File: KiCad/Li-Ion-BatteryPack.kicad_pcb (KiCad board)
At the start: 2 copper layers, 163.5 x 85.6 mm, 20 parts, among them J1 Charger, J2 Load, J3 Parallel, J4 BMS Sensor

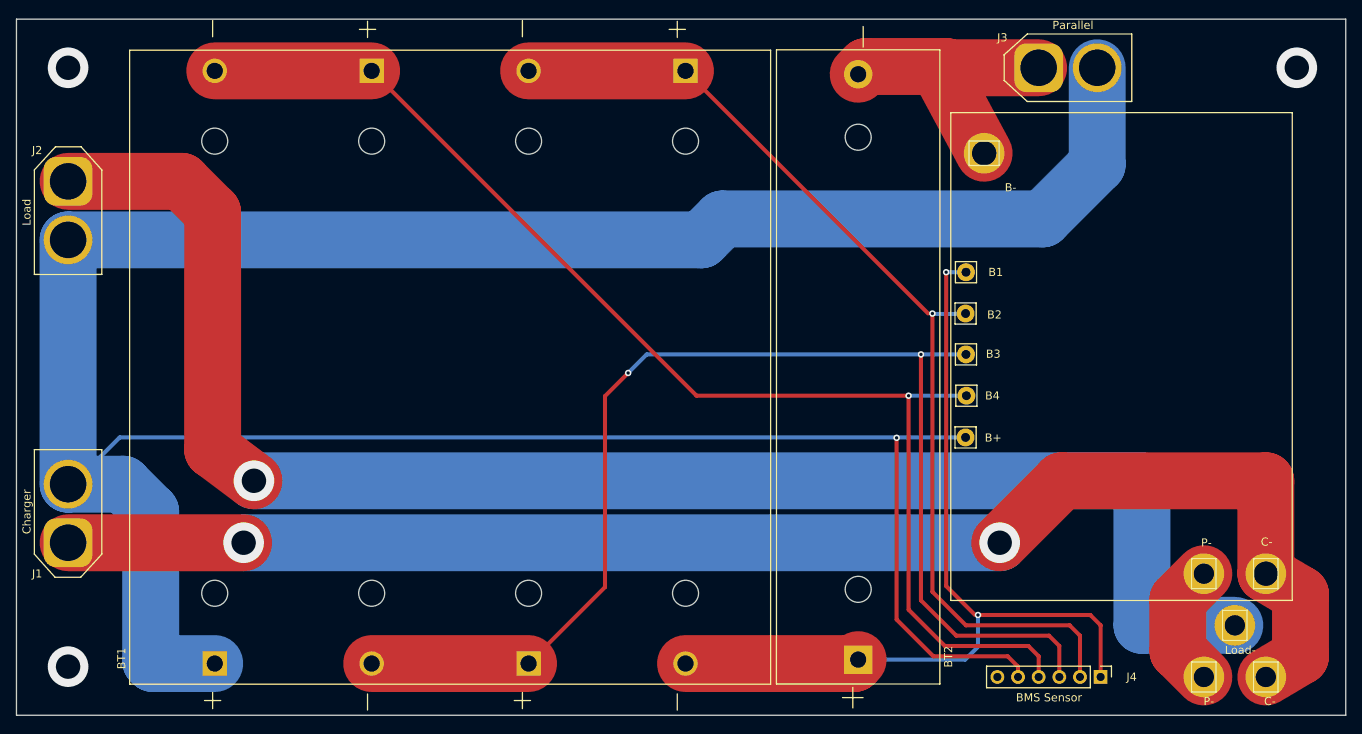
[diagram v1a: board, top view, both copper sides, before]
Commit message: Added some silkscreen objects to give better hints on wirering.
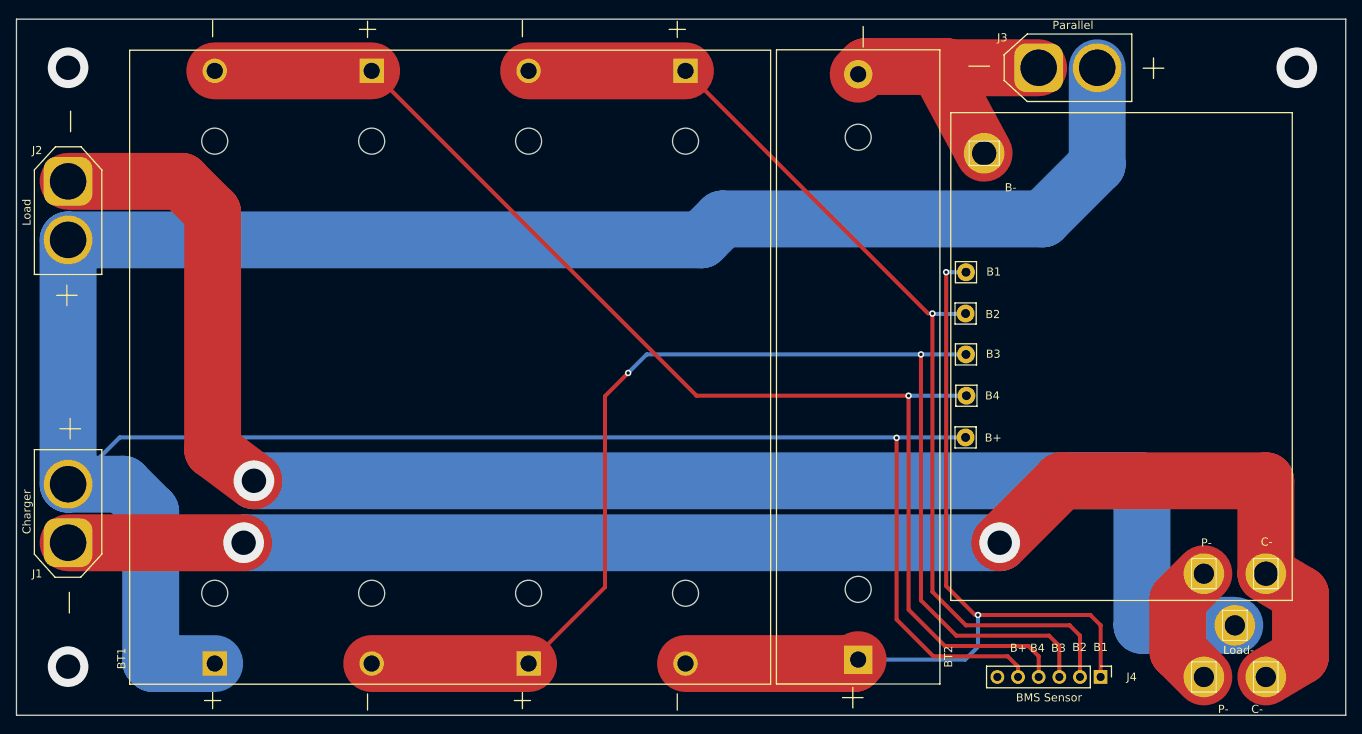
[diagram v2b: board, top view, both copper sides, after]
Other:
- board text added: "B+"
- board text added: "B1"
- board text added: "B2"
- board text added: "B3"
- board text added: "B4"

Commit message: Flipped some high current connections to the back of the board.
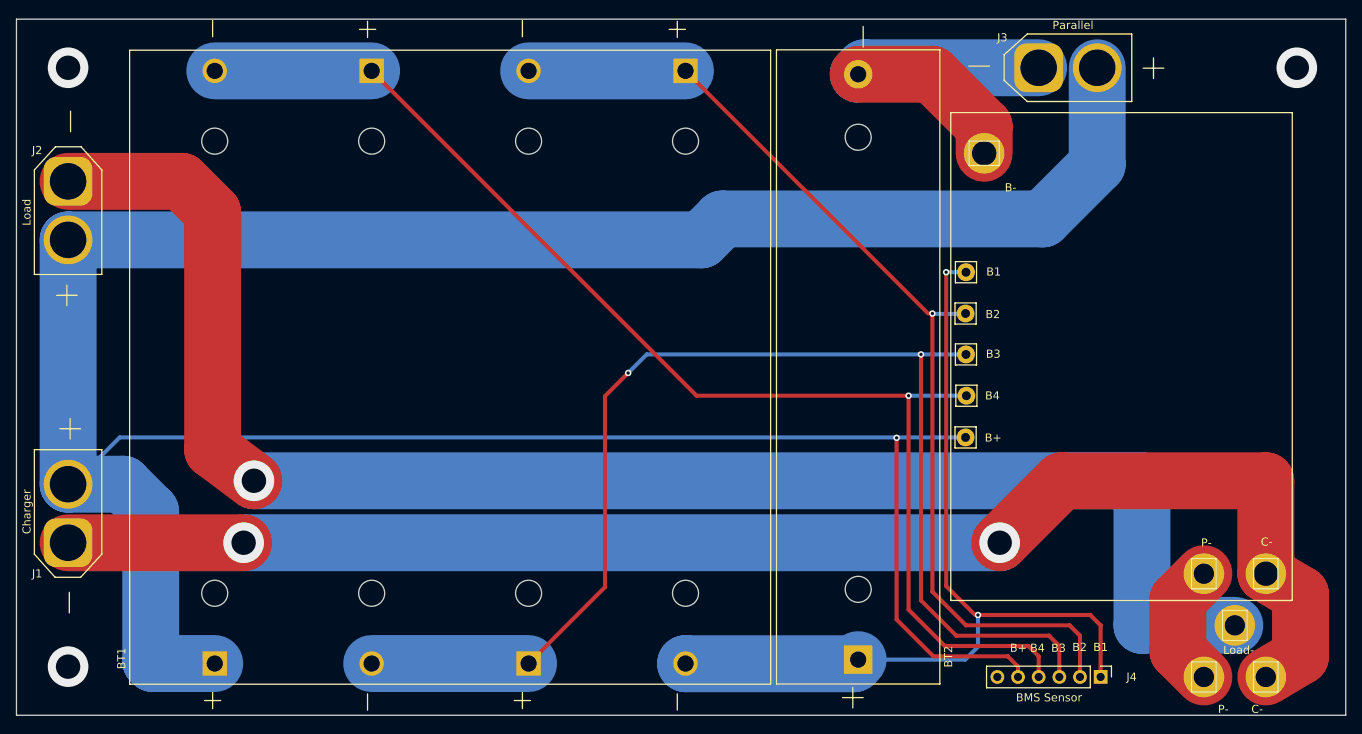
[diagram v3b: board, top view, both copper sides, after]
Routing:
- net Net-(BT2-Pad2): track 34.8 -> 44.0 mm
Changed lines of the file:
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@@
   (segment (start 147.74 77.05) (end 150.3172 74.4728) (width 7) (layer B.Cu) (net 1))
   (segment (start 69.85 77.05) (end 147.74 77.05) (width 7) (layer B.Cu) (net 1))
-  (segment (start 87.89 56.26) (end 107.19 56.26) (width 7) (layer F.Cu) (net 2))
   (via (at 173.228 96.2152) (size 0.8) (drill 0.4) (layers F.Cu B.Cu) (net 2))
   (segment (start 180.34 96.2152) (end 173.228 96.2152) (width 0.5) (layer B.Cu) (net 2))
@@
   (segment (start 173.228 122.5296) (end 177.6984 127) (width 0.5) (layer F.Cu) (net 2))
   (segment (start 173.228 96.2152) (end 173.228 122.5296) (width 0.5) (layer F.Cu) (net 2))
+  (segment (start 87.89 56.26) (end 107.19 56.26) (width 7) (layer B.Cu) (net 2))
   (via (at 138.7348 93.4212) (size 0.8) (drill 0.4) (layers F.Cu B.Cu) (net 3))
-  (segment (start 107.19 129.16) (end 126.49 129.16) (width 7) (layer F.Cu) (net 3))
+  (segment (start 107.19 129.16) (end 126.49 129.16) (width 7) (layer B.Cu) (net 3))
   (via (at 174.752 91.1352) (size 0.8) (drill 0.4) (layers F.Cu B.Cu) (net 3))
   (segment (start 191.77 127) (end 191.77 130.81) (width 0.5) (layer F.Cu) (net 3))
@@
   (segment (start 141.0208 91.1352) (end 138.7348 93.4212) (width 0.5) (layer B.Cu) (net 3))
   (segment (start 180.2892 91.1352) (end 141.0208 91.1352) (width 0.5) (layer B.Cu) (net 3))
-  (segment (start 145.79 56.26) (end 126.49 56.26) (width 7) (layer F.Cu) (net 4))
+  (segment (start 145.79 56.26) (end 126.49 56.26) (width 7) (layer B.Cu) (net 4))
   (segment (start 180.1876 86.1568) (end 176.3776 86.1568) (width 0.5) (layer B.Cu) (net 4))
   (via (at 176.16059 86.106) (size 0.8) (drill 0.4) (layers F.Cu B.Cu) (net 4))
@@
   (segment (start 177.8508 119.634) (end 181.4068 123.19) (width 0.5) (layer F.Cu) (net 5))
   (segment (start 177.8508 81.026) (end 177.8508 119.634) (width 0.5) (layer F.Cu) (net 5))
-  (segment (start 166.5468 129.16) (end 167.0304 128.6764) (width 7) (layer F.Cu) (net 5))
-  (segment (start 145.79 129.16) (end 166.5468 129.16) (width 7) (layer F.Cu) (net 5))
   (segment (start 181.7624 127) (end 181.7624 123.19) (width 0.5) (layer B.Cu) (net 5))
   (segment (start 181.7624 127.1016) (end 181.7624 127) (width 0.25) (layer B.Cu) (net 5))
@@
   (segment (start 195.58 123.19) (end 196.85 124.46) (width 0.5) (layer F.Cu) (net 5))
   (segment (start 181.7624 123.19) (end 195.58 123.19) (width 0.5) (layer F.Cu) (net 5))
-  (segment (start 178.01 55.88) (end 177.27 56.62) (width 5) (layer F.Cu) (net 6))
-  (segment (start 189.23 55.88) (end 178.01 55.88) (width 7) (layer F.Cu) (net 6))
-  (segment (start 177.27 56.62) (end 182.5244 66.3956) (width 7) (layer F.Cu) (net 6))
-  (segment (start 177.8576 55.7276) (end 178.01 55.88) (width 7) (layer F.Cu) (net 6))
-  (segment (start 167.9792 55.7276) (end 177.8576 55.7276) (width 7) (layer F.Cu) (net 6))
-  (segment (start 167.0304 56.6764) (end 167.9792 55.7276) (width 7) (layer F.Cu) (net 6))
+  (segment (start 166.5224 129.1844) (end 167.0304 128.6764) (width 7) (layer B.Cu) (net 5))
+  (segment (start 145.8144 129.1844) (end 166.5224 129.1844) (width 7) (layer B.Cu) (net 5))
+  (segment (start 145.79 129.16) (end 145.8144 129.1844) (width 7) (layer B.Cu) (net 5))
+  (segment (start 167.8268 55.88) (end 167.0304 56.6764) (width 7) (layer B.Cu) (net 6))
+  (segment (start 189.23 55.88) (end 167.8268 55.88) (width 7) (layer B.Cu) (net 6))
+  (segment (start 182.5244 63.0936) (end 182.5244 66.3956) (width 7) (layer F.Cu) (net 6))
+  (segment (start 176.1072 56.6764) (end 182.5244 63.0936) (width 7) (layer F.Cu) (net 6))
+  (segment (start 167.0304 56.6764) (end 176.1072 56.6764) (width 7) (layer F.Cu) (net 6))
   (via (at 91.44 114.3) (size 5) (drill 3) (layers F.Cu B.Cu) (net 7))
   (via (at 184.43501 114.3) (size 5) (drill 3) (layers F.Cu B.Cu) (net 7))
